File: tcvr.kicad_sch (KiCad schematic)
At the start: 48 parts, among them J1 Jack, J2 Ellensúly, J3 9V DC, Q1 BC817, Q2 2N7002, Q3 PZT2222A, SW1 billentyű, U1 LM386, Y1 3579kHz

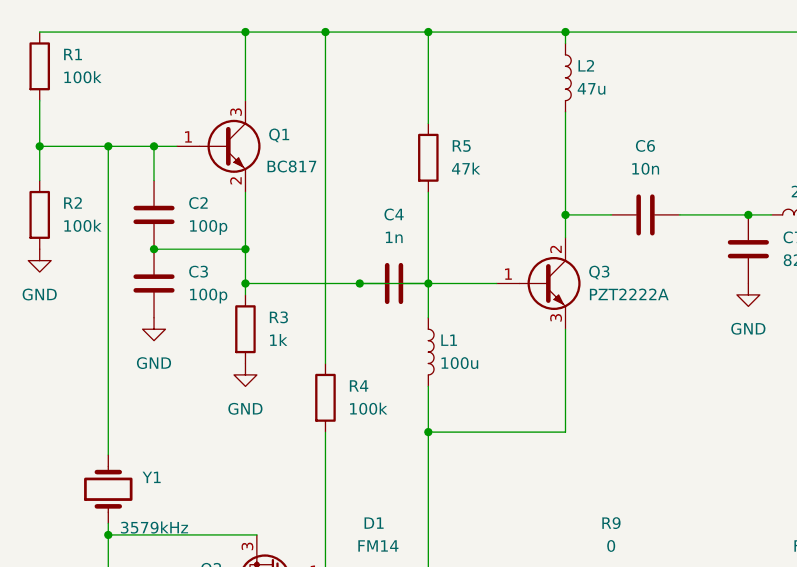
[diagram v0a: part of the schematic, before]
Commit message: átkötött kondi javítva a kapcsrajzban, layouton még hibás
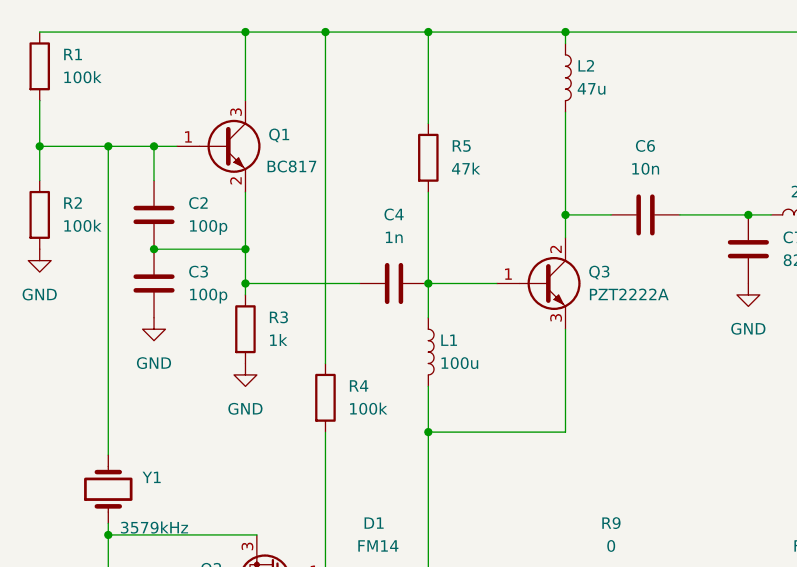
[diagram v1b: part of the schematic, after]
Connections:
- net at C2.2, C3.1, C4.1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: no longer C4.2, L1.1, Q3.1 (B), R5.2
- new net: C4.2, L1.1, Q3.1 (B), R5.2
